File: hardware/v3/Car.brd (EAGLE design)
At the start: 83.8 x 53.3 mm, 56 parts, among them IC1 PIC24FJ64GB204

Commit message: Started layout for v3.
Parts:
- removed 3V3: LM317, misc:SOT23
- removed C1: 10u, rcl:C1206
- removed C2, C3, C4, C5, PSB3: 100n, rcl:C0805
- removed C7, PSB2: 1u, rcl:C1206
- removed PSB1: 100u, SparkFun-Passives:PANASONIC_C
- removed R15: 240, rcl:R0805
- removed R16: 390, rcl:R0805
- removed RL1, RL2: 2k, rcl:R0805
- removed RN1: 10k, rcl:R0805
- added C11: 100u, SparkFun-Passives:PANASONIC_C
- added C12, C14, C16, C21: 10u, rcl:C1206
- added C13, C15, C17, C22, C23, C24, C41: 100n, rcl:C0805
- added CN1: (no value), SmslsTron-1:USB-MINIB
- added D1: (no value), SmslsTron-1:SMA
- added IC2: LD117AS50TR, v-reg:SOT223
- added IC3: LD117AS33TR, v-reg:SOT223
- added JP5: (no value), SmslsTron-1:1X04
- added R11, R22: 2k, rcl:R0805
- added R21: 10k, rcl:R0805
- added R23, R25: 1k, rcl:R0805
- added R24, R26: 100, rcl:R0805
- added S1: SWITCH-MOMENTARY-2SMD-4, SmslsTron-1:TACTILE_SWITCH_TALL
- added T1, T2: (no value), SmslsTron-1:SOT-23
- added U$1: FUSE24X06, SmslsTron-1:2SMD-24X06
- 11RS, 12RS, 21RS, 22RS: device resistor:R2512 -> resistor:R1210
- moved 11RT 39.5 mm to (43.8, 32.4)
- moved 22RT 39.1 mm to (43.8, 21.6)
- moved 21RT 39.0 mm to (43.2, 12.7)
- moved 12RT 38.7 mm to (43.8, 41.3)
- moved 11CT 34.6 mm to (46.4, 32.4)
- moved 22CT 34.1 mm to (46.4, 21.6)
- moved 21CT 34.0 mm to (45.7, 12.7)
- moved 12CT 33.7 mm to (46.4, 41.3)
- moved 11CC 25.7 mm to (55.9, 27.9), turned to 180 degrees
- moved 1LGB 25.7 mm to (50.2, 27.9)
- moved 22CC 24.3 mm to (55.9, 25.4), turned to 180 degrees
- moved 12CC 21.1 mm to (55.9, 45.1), turned to 180 degrees
- moved 11RS 20.6 mm to (67.9, 30.5), turned to 180 degrees
- moved 21CC 20.3 mm to (56.5, 7.62), turned to 180 degrees
- moved 22RS 19.7 mm to (67.9, 24.8), turned to 180 degrees
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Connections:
- removed net 12V: 1LDB.1, 1LDC.+, 2LDB.1, 2LDC.+, 3V3.3, J1.1, MD1.24, MD2.24, PSB1.+, PSB2.1, PSB3.1
- removed net 3V3: 3V3.2, 3V3.4, C2.1, C3.1, C4.1, C5.1, C7.1, IC1.10, IC1.17, IC1.28, IC1.40, IC1.6, ICD.2, JP2.4, MOUTH.9, PWR.A, R15.2, RN1.1
- removed net 5V: 1LGB.1, 2LGB.1, MD1.13, MD2.13
- removed net A7: HB.A
- removed net D12/M2_P1: MD2.16
- removed net D13/M2_P2: MD2.10
- removed net D13/SCK: JP4.6
- removed net D14/M2_I0X: MD2.20, MD2.8
- removed net D15/M2_I1X: MD2.17, MD2.9
- removed net D4/M1_P2: MD1.10
- removed net D7/M1_I0X: MD1.20, MD1.8
- removed net D8/M1_I1X: MD1.17, MD1.9
- removed net DGND: MD1.18, MD1.19, MD1.6, MD1.7, MD2.18, MD2.19, MD2.6, MD2.7
- removed net M1_I00: IC1.34
- removed net M1_I10: IC1.32
- removed net M1_V1: MD1.15
- removed net M1_V2: MD1.11
- removed net M2_I00: IC1.12
- removed net M2_I10: IC1.26
- removed net M2_V1: MD2.15
- removed net M2_V2: MD2.11
- removed net MISO: MOUTH.1
- removed net MOSI: MOUTH.12
- removed net SCLK: MOUTH.13
- removed net VCAP: IC1.7
- new net +3V3: C16.1, C17.1, C22.1, C23.1, C24.1, C41.1, IC1.10, IC1.17, IC1.28, IC1.40, IC1.6, IC3.2, IC3.4, ICD.2, JP2.4, MOUTH.9, PWR.A, R21.1
- new net +5V: 1LGB.1, 2LGB.1, C14.1, C15.1, IC2.2, IC2.4, IC3.3, JP2.5, JP5.1, MD1.13, MD2.13, R24.2, R26.2
- new net A4_PO: JP5.2, T1.2
- new net A5_PO: JP5.3, T2.2
- new net M1_I02: IC1.32, MD1.8
- new net M1_I12: IC1.35, MD1.9
- new net M2_I02: IC1.42, MD2.8
- new net M2_I12: IC1.43, MD2.9
- new net N$12: R26.1, T2.1
- new net N$19: R23.2, T1.3
- new net N$3: D1.A, U$1.P$2
- new net N$7: R24.1, T1.1
- new net VBUS: CN1.VBUS
- new net VIN_PRF: J1.1, U$1.P$1
- net /RST: now also R21.2, S1.A2; no longer RN1.2
- net A4: now also R23.1
- net A5: now also R25.1
- net D10/M2_PWM2: now also MD2.11
- net D11/MOSI: now also MOUTH.12
- net D12/MISO: now also MOUTH.1
- net D13/SCLK: now also HB.A, JP4.6, MOUTH.13
- net D3/M1_P2: now also MD1.10
- net D4/M2_P1: now also MD2.16
- net D5/M1_PWM1: now also MD1.15
- net D6/M1_PWM2: now also MD1.11
- net D7/M2_P2: now also MD2.10
- net D9/M2_PWM1: now also MD2.15
- net GND: now also C11.-, C12.2, C13.2, C14.2, C15.2, C16.2, C17.2, C21.2, C22.2, C23.2, C24.2, C41.2, CN1.GND, IC2.1, IC3.1, JP5.4, MD1.18, MD1.19, MD1.6, MD1.7, MD2.18, MD2.19, MD2.6, MD2.7, R11.2, R22.2, S1.B2; no longer C1.2, C2.2, C3.2, C4.2, C5.2, C7.2, PSB1.-, PSB2.2, PSB3.2, R16.1, RL1.2, RL2.2
- net M1_I01: now also IC1.34, MD1.20; no longer IC1.13
- net M1_I11: now also IC1.13, MD1.17; no longer IC1.35
- net M2_I01: now also IC1.12, MD2.20; no longer IC1.15
- net M2_I11: now also IC1.15, MD2.17; no longer IC1.27
- net N$20: now also R25.2, T2.3; no longer 3V3.1, R15.1, R16.2
- net N$40: now also C21.1, IC1.7; no longer C1.1
- net N$46: now also R22.1; no longer RL1.1
- net N$65: now also R11.1; no longer RL2.1
- net RFM_CS: now also IC1.27; no longer IC1.43
- net RFM_IRQ: now also IC1.26; no longer IC1.42
- net VIN: now also 1LDB.1, 1LDC.+, 2LDB.1, 2LDC.+, C11.+, C12.1, C13.1, D1.C, IC2.3, MD1.24, MD2.24
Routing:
- net GND: track 0.00 -> 314.9 mm, vias 0 -> 32
- net VIN: track 0.00 -> 162.4 mm, vias 0 -> 12
- net +5V: track 0.00 -> 50.0 mm, vias 0 -> 3
- net N$6: track 0.00 -> 25.0 mm, vias 0 -> 1
- net N$9: track 0.00 -> 24.6 mm, vias 0 -> 1
- net N$8: track 0.00 -> 23.9 mm, vias 0 -> 1
- net N$10: track 0.00 -> 18.6 mm, vias 0 -> 1
- net N$18: track 0.00 -> 10.8 mm
- net N$16: track 0.00 -> 10.3 mm
- net N$13: track 0.00 -> 9.92 mm
- net VIN_PRF: track 0.00 -> 7.98 mm
- net N$14: track 0.00 -> 7.42 mm
- net N$3: track 0.00 -> 6.62 mm
- net +3V3: track 0.00 -> 6.30 mm
- net N$17: track 0.00 -> 6.08 mm
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- added copper zone on layer 1, net +5V
- added copper zone on layer 1, net GND
- added copper zone on layer 16, net GND
- added copper zone on layer 1, net VIN
- added copper zone on layer 16, net VIN
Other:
- board size 83.8 x 53.3 mm -> 80.6 x 53.3 mm
- board text added: "3v3"
- board text added: "PGC"
- board text added: "PGD"
- board text added: "RST"
- board text removed: "-"
- board text removed: "--"

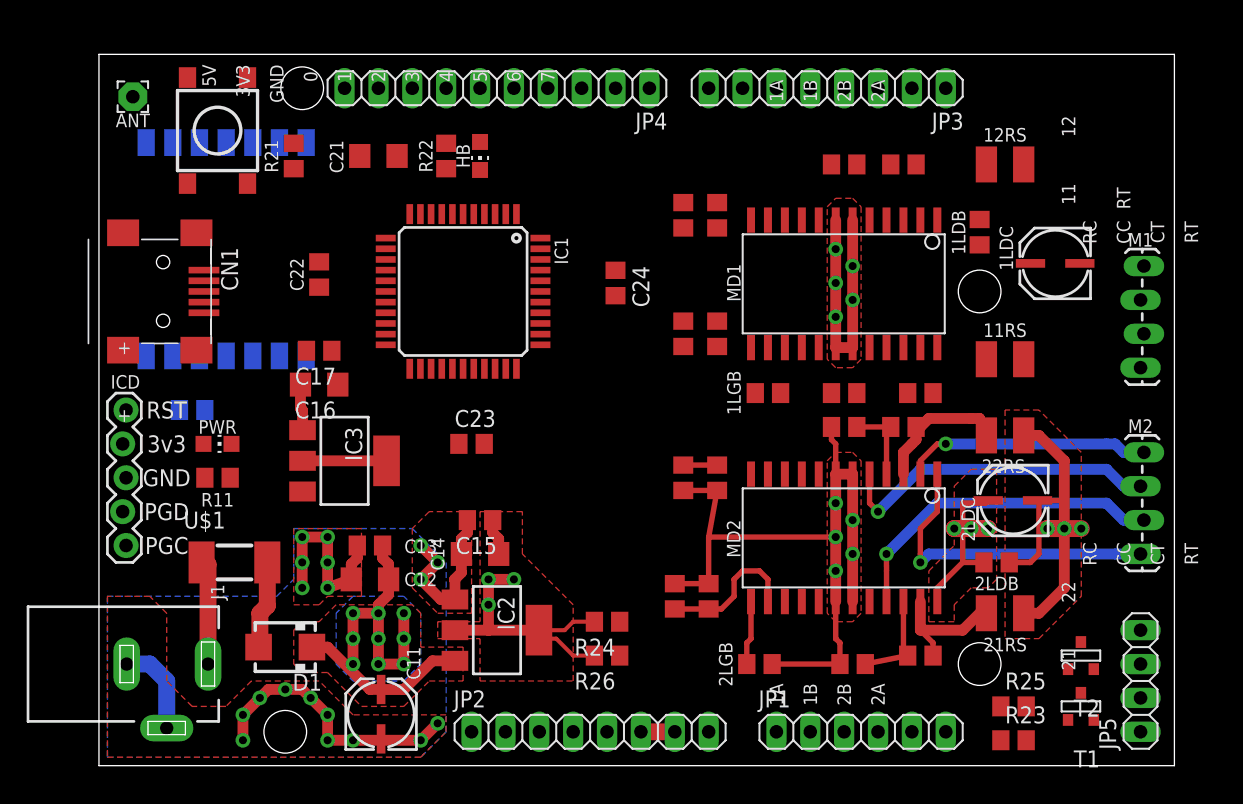
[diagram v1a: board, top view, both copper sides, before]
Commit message: Continued working layout. Added USB components. Remapped some pins.
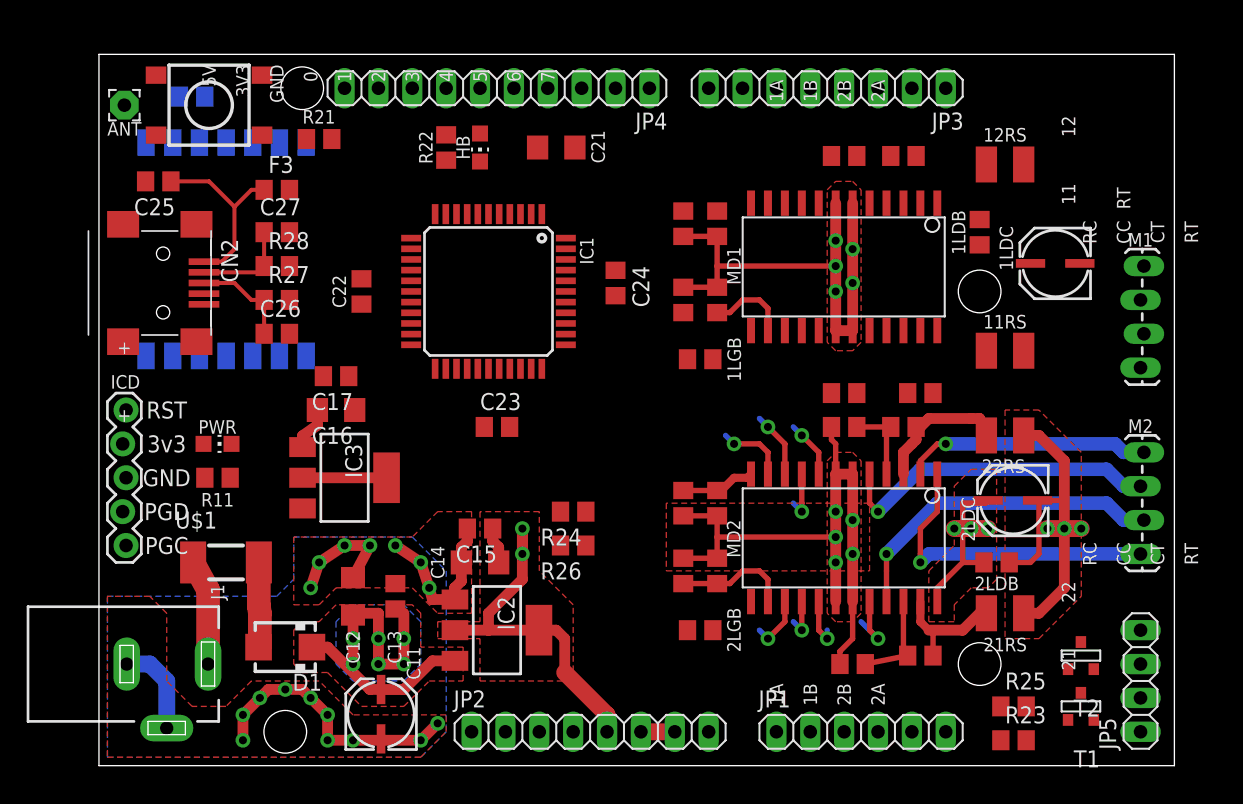
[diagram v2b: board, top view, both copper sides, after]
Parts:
- removed CN1: (no value), SmslsTron-1:USB-MINIB
- added C25: 10n, rcl:C0805
- added C26, C27: 47p, rcl:C0805
- added CN2: (no value), adafruit:USB-MINIB
- added F3: FERRITE0805, SMSLS:0805
- added R27, R28: 27, resistor:R0805
- moved C41 23.5 mm to (6.99, 50.2), turned to 180 degrees
- moved C21 13.4 mm to (34.3, 46.4), turned to 0 degrees
- moved R24 8.64 mm to (35.6, 19.1)
- moved R26 8.64 mm to (35.6, 16.5)
- moved 1LGB 5.68 mm to (45.1, 30.5), turned to 180 degrees
- moved 2LGB 5.12 mm to (45.1, 10.2), turned to 180 degrees
- moved C13 4.26 mm to (22.2, 12.7), turned to 90 degrees
- moved C22 3.42 mm to (19.7, 35.6)
- moved 11CT 2.54 mm to (46.4, 34.9)
- moved 11RT 2.54 mm to (43.8, 34.9)
- moved R21 2.29 mm to (16.5, 47.0), turned to 180 degrees
- moved C16 2.29 mm to (17.8, 26.7)
- moved C17 2.29 mm to (17.8, 29.2)
- moved C23 2.29 mm to (29.8, 25.4)
- moved S1 2.01 mm to (8.26, 49.5), turned to 0 degrees
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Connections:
- net A4 renamed A4/SDA
- net A5 renamed A5/SCL
- net D0 renamed D0/RXD
- net D1 renamed D1/TXD
- removed net D8: IC1.25, JP4.1
- removed net RFM_IRQ: IC1.26, MOUTH.2
- new net D8/RFM_IRQ: IC1.26, JP4.1, MOUTH.2
- new net N$21: C26.1, CN2.D+, R27.1
- new net N$22: C27.1, CN2.D-, R28.1
- new net VBUS-PRF: C25.1, CN2.VBUS, F3.1
- net GND: now also C25.2, C26.2, C27.2, CN2.GND; no longer CN1.GND
- net M2_I02: now also IC1.25; no longer IC1.42
- net USBD+: now also R27.2
- net USBD-: now also R28.2
- net VBUS: now also F3.2, IC1.42; no longer CN1.VBUS
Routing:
- net GND: track 314.9 -> 405.4 mm, vias 32 -> 30
- net VBUS-PRF: track 0.00 -> 14.2 mm
- net N$21: track 0.00 -> 7.58 mm
- net N$22: track 0.00 -> 7.52 mm
- net N$41: track 0.00 -> 6.13 mm
- net D10/M2_PWM2: track 0.00 -> 5.34 mm, vias 0 -> 1
- net VIN: track 162.4 -> 167.6 mm, vias 12 -> 9
- net D7/M2_P2: track 0.00 -> 4.96 mm, vias 0 -> 1
- net M2_I01: track 0.00 -> 4.84 mm, vias 0 -> 1
- net M2_I02: track 0.00 -> 4.33 mm, vias 0 -> 1
- net D9/M2_PWM1: track 0.00 -> 4.20 mm, vias 0 -> 1
- net M2_I12: track 0.00 -> 3.71 mm, vias 0 -> 1
- net M2_I11: track 0.00 -> 3.67 mm, vias 0 -> 1
- net N$15: track 2.54 -> 5.59 mm
- net D4/M2_P1: track 0.00 -> 3.04 mm, vias 0 -> 1
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- added copper zone on layer 2, net GND
- added copper zone on layer 15, net VIN

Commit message: More routing (~50% complete). Normalized/placed texts.
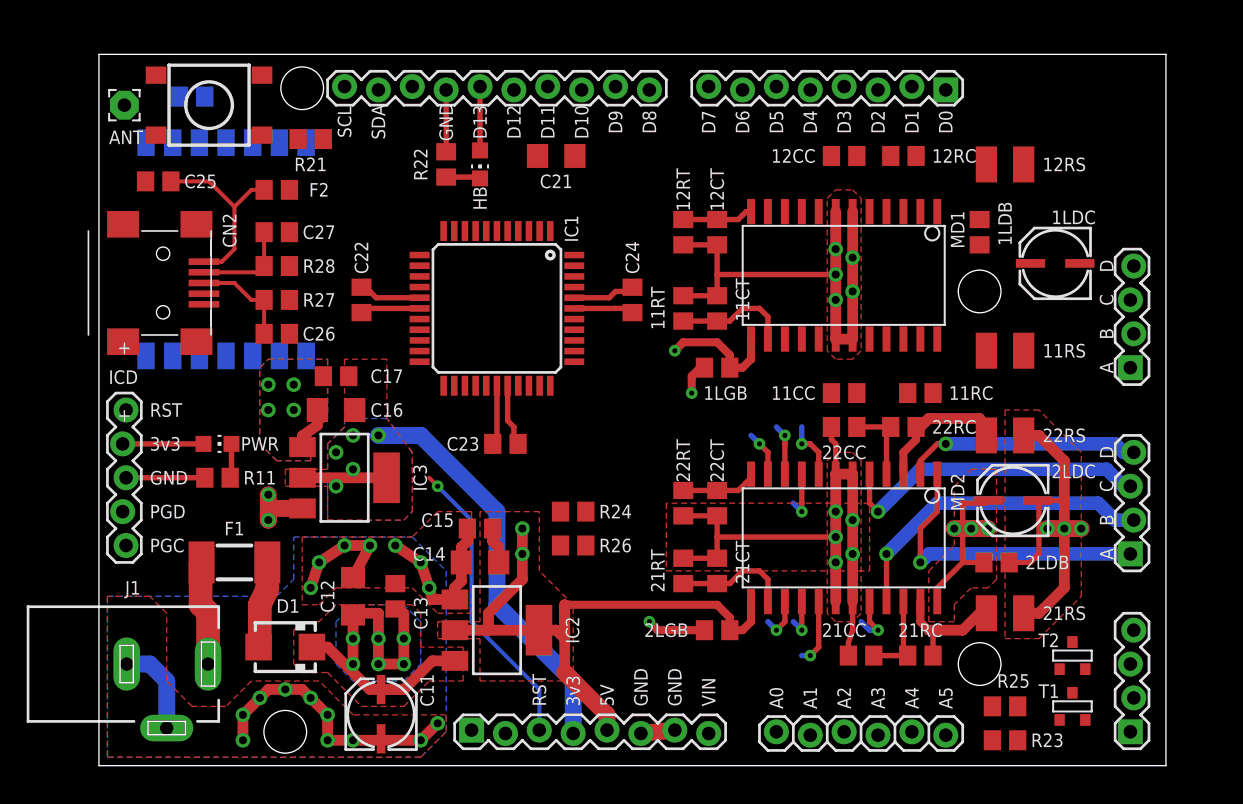
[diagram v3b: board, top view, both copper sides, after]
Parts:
- removed JP2, JP3: (no value), pinhead:1X08
- removed JP4: (no value), pinhead:1X10
- removed JP5: (no value), SmslsTron-1:1X04
- removed U$1: FUSE24X06, SmslsTron-1:2SMD-24X06
- added F1: FUSE24X06, SmslsTron-1:2SMD-24X06
- added JP6, JP7: (no value), SparkFun-Connectors:1X08_LOCK
- added JP8: (no value), SparkFun-Connectors:1X10_LOCK
- added JP9: (no value), SparkFun-Connectors:1X06_LOCK
- JP1: device pinhead:1X06 -> SparkFun-Connectors:1X04_LOCK
- M1, M2: device SparkFun-Connectors:1X04_LOCK_LONGPADS -> SparkFun-Connectors:1X04_LOCK
- moved JP1 20.3 mm to (77.5, 2.54), turned to 90 degrees
- moved C24 1.80 mm to (40.0, 34.9)
- moved IC1 1.42 mm to (29.8, 34.3)
- moved C23 1.42 mm to (30.5, 24.1)
- moved 1LGB 1.42 mm to (46.4, 29.8)
- moved 2LGB 1.27 mm to (46.4, 10.2)
- moved HB 1.27 mm to (28.6, 45.1)
- moved R22 1.27 mm to (26.0, 45.1)
- moved 21CC 0.90 mm to (57.1, 8.26)
- moved C22 0.64 mm to (19.7, 34.9)
- moved M1 0.64 mm to (77.5, 29.8)
- moved M2 0.64 mm to (77.5, 15.9)
- moved MD1 0.64 mm to (55.9, 36.8)
- moved R23 0.64 mm to (67.9, 1.91)
- moved R25 0.64 mm to (67.9, 4.45)
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- renumbered F3 to F2
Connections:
- net +3V3: now also JP6.4; no longer JP2.4
- net +5V: now also JP1.1, JP6.5; no longer JP2.5, JP5.1
- net /RST: now also JP6.3; no longer JP2.3
- net A0: now also JP9.1; no longer JP1.1
- net A1: now also JP9.2; no longer JP1.2
- net A2: now also JP9.3; no longer JP1.3
- net A3: now also JP9.4; no longer JP1.4
- net A4/SDA: now also JP8.9, JP9.5; no longer JP1.5, JP4.9
- net A4_PO: now also JP1.2; no longer JP5.2
- net A5/SCL: now also JP8.10, JP9.6; no longer JP1.6, JP4.10
- net A5_PO: now also JP1.3; no longer JP5.3
- net D0/RXD: now also JP7.1; no longer JP3.1
- net D1/TXD: now also JP7.2; no longer JP3.2
- net D10/M2_PWM2: now also JP8.3; no longer JP4.3
- net D11/MOSI: now also JP8.4; no longer JP4.4
- net D12/MISO: now also JP8.5; no longer JP4.5
- net D13/SCLK: now also JP8.6; no longer JP4.6
- net D2/M1_P1: now also JP7.3; no longer JP3.3
- net D3/M1_P2: now also JP7.4; no longer JP3.4
- net D4/M2_P1: now also JP7.5; no longer JP3.5
- net D5/M1_PWM1: now also JP7.6; no longer JP3.6
- net D6/M1_PWM2: now also JP7.7; no longer JP3.7
- net D7/M2_P2: now also JP7.8; no longer JP3.8
- net D8/RFM_IRQ: now also JP8.1; no longer JP4.1
- net D9/M2_PWM1: now also JP8.2; no longer JP4.2
- net GND: now also JP1.4, JP6.6, JP6.7, JP8.7; no longer JP2.6, JP2.7, JP4.7, JP5.4
- net N$3: now also F1.P$2; no longer U$1.P$2
- net VIN: now also JP6.8; no longer JP2.8
- net VIN_PRF: now also F1.P$1; no longer U$1.P$1
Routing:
- net +3V3: track 6.30 -> 72.6 mm, vias 0 -> 5
- net +5V: track 52.1 -> 114.2 mm, vias 2 -> 5
- net GND: track 405.4 -> 453.9 mm, vias 30 -> 36
- net /RST: track 0.00 -> 22.3 mm, vias 0 -> 1
- net N$42: track 0.00 -> 5.33 mm
- net D13/SCLK: track 0.00 -> 4.79 mm
- net N$46: track 0.00 -> 2.58 mm
- net N$65: track 0.00 -> 2.58 mm
- net N$41: track 6.13 -> 8.67 mm
- net D10/M2_PWM2: track 5.34 -> 3.43 mm
- net VIN: track 167.6 -> 166.0 mm
- net M2_I11: track 3.67 -> 4.95 mm
- net D7/M2_P2: track 4.96 -> 3.80 mm
- net M2_I01: track 4.84 -> 3.94 mm
- net D9/M2_PWM1: track 4.20 -> 3.30 mm
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- added copper zone on layer 1, net +3V3
- added copper zone on layer 16, net +3V3
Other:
- board size 80.6 x 53.3 mm -> 80 x 53.3 mm
- board text added: "A"
- board text added: "A0"
- board text added: "A1"
- board text added: "A2"
- board text added: "A3"
- board text added: "A4"
- board text added: "A5"
- board text added: "B"
- board text added: "C"
- board text added: "D"
- board text added: "D0"
- board text added: "D1"
- board text added: "D10"
- board text added: "D11"
- board text added: "D12"
- board text added: "D13"
- board text added: "D2"
- board text added: "D3"
- board text added: "D4"
- board text added: "D5"
- board text added: "D6"
- board text added: "D7"
- board text added: "D8"
- board text added: "D9"
- board text added: "SCL"
- board text added: "SDA"
- board text added: "VIN"
- board text removed: "0"
- board text removed: "1"
- board text removed: "11"
- board text removed: "12"
- board text removed: "1A"
- board text removed: "1B"
- board text removed: "2"
- board text removed: "21"
- board text removed: "22"
- board text removed: "2A"
- board text removed: "2B"
- board text removed: "3"
- board text removed: "3V3"
- board text removed: "4"
- board text removed: "5"
- board text removed: "6"
- board text removed: "7"
- board text removed: "CC"
- board text removed: "CT"
- board text removed: "RC"
- board text removed: "RT"
